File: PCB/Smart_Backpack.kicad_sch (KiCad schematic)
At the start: 5 parts, among them U1 ESP32-PICO-MINI-02-N8R2

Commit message: Add files via upload
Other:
- added sheet Components (untitled.kicad_sch)
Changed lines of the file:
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@@
+		)
+	)
+	(sheet
+		(at 208.28 21.59)
+		(size 13.97 7.62)
+		(exclude_from_sim no)
+		(in_bom yes)
+		(on_board yes)
+		(dnp no)
+		(fields_autoplaced yes)
+		(stroke
+			(width 0.1524)
+			(type solid)
+		)
+		(fill
+			(color 0 0 0 0.0000)
+		)
+		(property "Sheetname" "Components"
+			(at 208.28 20.8784 0)
+			(effects
+				(font
+					(size 1.27 1.27)
+				)
+				(justify left bottom)
+			)
+		)
+		(property "Sheetfile" "untitled.kicad_sch"
+			(at 208.28 29.7946 0)
+			(effects
+				(font
+					(size 1.27 1.27)
+				)
+				(justify left top)
+			)
+		)
+		(instances
+			(project "Smart_Backpack"
+				(path "/38abc652-c887-4ef7-a45f-d93ca7f4b2d6"
+					(page "3")
+				)
+			)
 		)
 	)

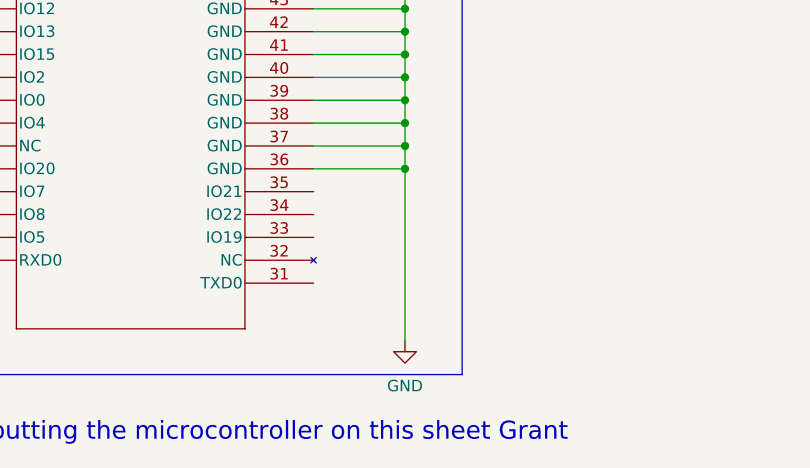
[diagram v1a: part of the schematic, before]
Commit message: Added IMU footprint/symbol
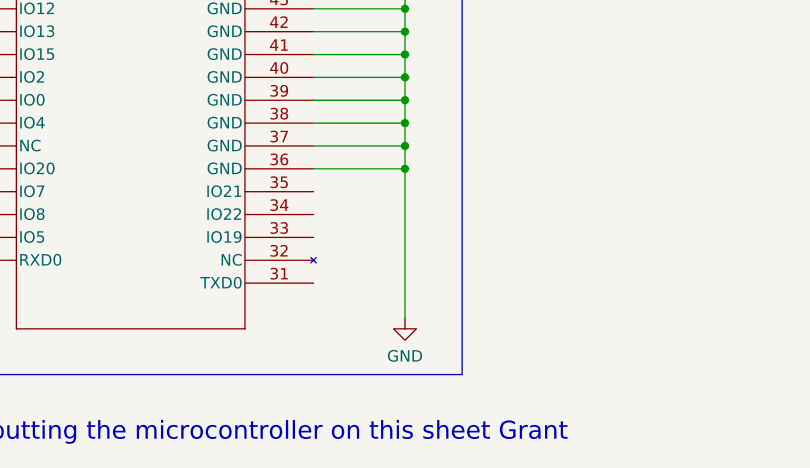
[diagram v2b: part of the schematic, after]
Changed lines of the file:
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@@
 	(wire
 		(pts
-			(xy 78.74 118.11) (xy 78.74 99.06)
+			(xy 78.74 115.57) (xy 78.74 99.06)
 		)
 		(stroke
@@
 	(symbol
 		(lib_id "power:GND")
-		(at 78.74 118.11 0)
+		(at 78.74 115.57 0)
 		(unit 1)
 		(exclude_from_sim no)
@@
 		(on_board yes)
 		(dnp no)
-		(fields_autoplaced yes)
 		(property "Reference" "#PWR02"
-			(at 78.74 124.46 0)
+			(at 78.74 121.92 0)
 			(effects
 				(font
@@
 		)
 		(property "Value" "GND"
-			(at 78.74 123.19 0)
+			(at 78.74 119.888 0)
 			(effects
 				(font
@@
 		)
 		(property "Footprint" ""
-			(at 78.74 118.11 0)
+			(at 78.74 115.57 0)
 			(effects
 				(font
@@
 		)
 		(property "Datasheet" ""
-			(at 78.74 118.11 0)
+			(at 78.74 115.57 0)
 			(effects
 				(font
@@
 		)
 		(property "Description" ""
-			(at 78.74 118.11 0)
-			(effects
-				(font
+			(at 78.74 115.57 0)
+			(effects
+				(font

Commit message: update todo list
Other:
- note added: "Fix Power circuit add reset pin"
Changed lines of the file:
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@@
+		)
+	)
+	(text "Fix Power circuit add reset pin"
+		(exclude_from_sim no)
+		(at 197.866 93.218 0)
+		(effects
+			(font
+				(size 1.27 1.27)
+			)
+			(justify left bottom)
 		)
 	)

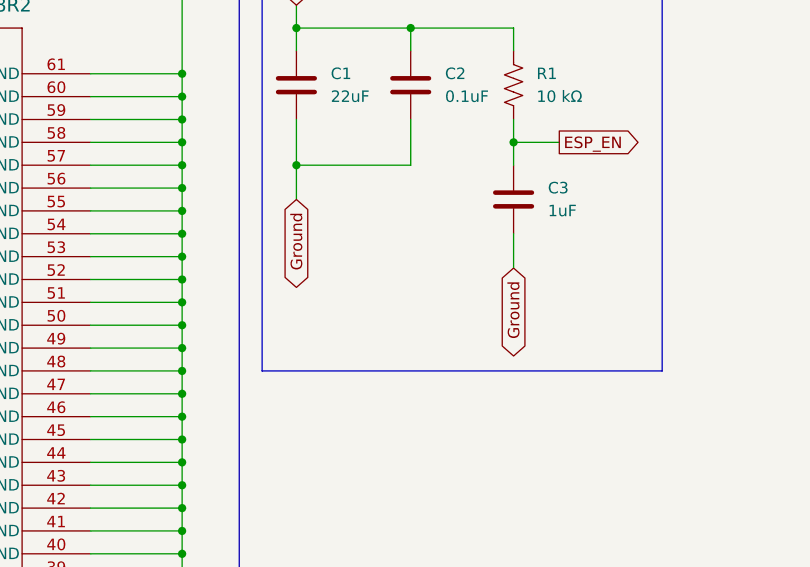
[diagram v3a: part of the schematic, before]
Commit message: Just changed some ground pins to ground
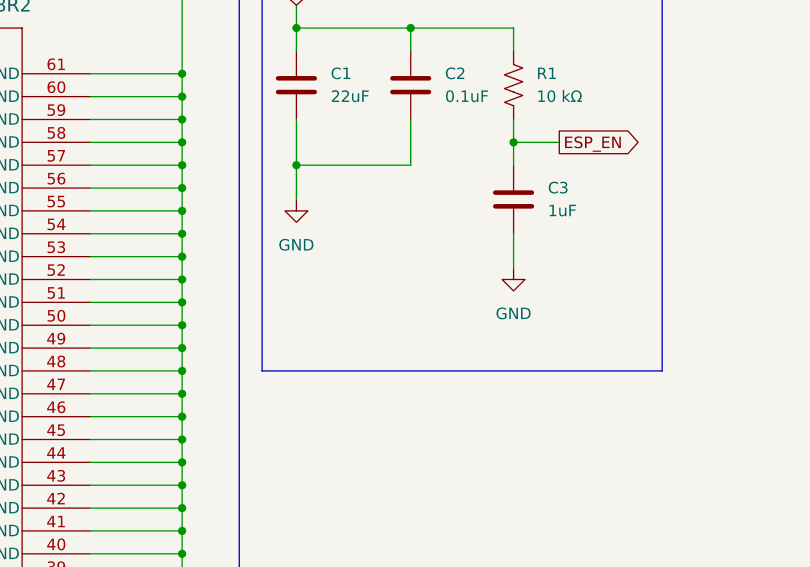
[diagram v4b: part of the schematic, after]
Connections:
- net Ground is gone; now on net GND: C1.2, C2.2, C3.2
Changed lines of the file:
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@@
 		)
 	)
-	(global_label "Ground"
-		(shape bidirectional)
-		(at 115.57 57.15 270)
+	(global_label "Buck_3v3"
+		(shape input)
+		(at 27.94 40.64 180)
 		(fields_autoplaced yes)
 		(effects
@@
 		)
 		(property "Intersheetrefs" "${INTERSHEET_REFS}"
-			(at 115.57 67.8987 90)
+			(at 16.0649 40.64 0)
 			(effects
 				(font
@@
 		)
 	)
-	(global_label "Ground"
-		(shape bidirectional)
-		(at 91.44 49.53 270)
+	(global_label "Buck_3v3"
+		(shape input)
+		(at 91.44 27.94 90)
 		(fields_autoplaced yes)
 		(effects
@@
 				(size 1.27 1.27)
 			)
-			(justify right)
-		)
-		(property "Intersheetrefs" "${INTERSHEET_REFS}"
-			(at 91.44 60.2787 90)
-			(effects
-				(font
-					(size 1.27 1.27)
-				)
-				(justify right)
-				(hide yes)
-			)
-		)
-	)
-	(global_label "Buck_3v3"
-		(shape input)
-		(at 27.94 40.64 180)
-		(fields_autoplaced yes)
-		(effects
-			(font
-				(size 1.27 1.27)
-			)
-			(justify right)
-		)
-		(property "Intersheetrefs" "${INTERSHEET_REFS}"
-			(at 16.0649 40.64 0)
-			(effects
-				(font
-					(size 1.27 1.27)
-				)
-				(justify right)
-				(hide yes)
-			)
-		)
-	)
-	(global_label "Buck_3v3"
-		(shape input)
-		(at 91.44 27.94 90)
-		(fields_autoplaced yes)
-		(effects
-			(font
-				(size 1.27 1.27)
-			)
 			(justify left)
 		)
@@
 				(justify left)
 				(hide yes)
+			)
+		)
+	)
+	(symbol
+		(lib_name "GND_1")
+		(lib_id "power:GND")
+		(at 115.57 57.15 0)
+		(unit 1)
+		(exclude_from_sim no)
+		(in_bom yes)
+		(on_board yes)
+		(dnp no)
+		(fields_autoplaced yes)
+		(property "Reference" "#PWR06"
+			(at 115.57 63.5 0)
+			(effects
+				(font
+					(size 1.27 1.27)
+				)
+				(hide yes)
+			)
+		)
+		(property "Value" "GND"
+			(at 115.57 62.23 0)
+			(effects
+				(font
+					(size 1.27 1.27)
+				)
+			)
+		)
+		(property "Footprint" ""
+			(at 115.57 57.15 0)
+			(effects
+				(font
+					(size 1.27 1.27)
+				)
+				(hide yes)
+			)
+		)
+		(property "Datasheet" ""
+			(at 115.57 57.15 0)
+			(effects
+				(font
+					(size 1.27 1.27)
+				)
+				(hide yes)
+			)
+		)
+		(property "Description" "Power symbol creates a global label with name \"GND\" , ground"
+			(at 115.57 57.15 0)
+			(effects
+				(font
+					(size 1.27 1.27)
+				)
+				(hide yes)
+			)
+		)
+		(pin "1"
+		)
+		(instances
+			(project ""
+				(path "/38abc652-c887-4ef7-a45f-d93ca7f4b2d6"
+					(reference "#PWR06")
+					(unit 1)
+				)
 			)
 		)
@@
 					(unit 1)
 				)
+			)
+		)
+	)
+	(symbol
+		(lib_name "GND_1")
+		(lib_id "power:GND")
+		(at 91.44 49.53 0)
+		(unit 1)
+		(exclude_from_sim no)
+		(in_bom yes)
+		(on_board yes)
+		(dnp no)
+		(fields_autoplaced yes)
+		(property "Reference" "#PWR07"
+			(at 91.44 55.88 0)
+			(effects
+				(font
+					(size 1.27 1.27)
+				)
+				(hide yes)
+			)
+		)
+		(property "Value" "GND"
+			(at 91.44 54.61 0)
+			(effects
+				(font
+					(size 1.27 1.27)
+				)
+			)
+		)
+		(property "Footprint" ""
+			(at 91.44 49.53 0)
+			(effects
+				(font
+					(size 1.27 1.27)
+				)
+				(hide yes)
+			)
+		)
+		(property "Datasheet" ""
+			(at 91.44 49.53 0)
+			(effects
+				(font
+					(size 1.27 1.27)
+				)
+				(hide yes)
+			)
+		)
+		(property "Description" "Power symbol creates a global label with name \"GND\" , ground"
+			(at 91.44 49.53 0)
+			(effects
+				(font
+					(size 1.27 1.27)
+				)
+				(hide yes)
+			)
+		)
+		(pin "1"
+		)
+		(instances
+			(project "Smart_Backpack"
+				(path "/38abc652-c887-4ef7-a45f-d93ca7f4b2d6"
+					(reference "#PWR07")
+					(unit 1)
+				)

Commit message: Added micro footprint
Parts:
- removed U1: ESP32-PICO-MINI-02-N8R2, ESP32:ESP32-PICO-MINI-02_EXP, symbol ESP32:ESP32-PICO-MINI-02-N8R2
- added U3: ESP32-PICO-MINI-02-N8R2, STM32:ESP32-PICO-MINI-02_EXP, symbol ESP32:ESP32-PICO-MINI-02-N8R2
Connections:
- net Buck_3v3: now also U3.3 (3V3)
- net ESP_EN: now also U3.8 (EN)
- net GND: now also U3.1 (GND), U3.11 (GND), U3.14 (GND), U3.2 (GND), U3.36 (GND), U3.37 (GND), U3.38 (GND), U3.39 (GND), U3.40 (GND), U3.41 (GND), U3.42 (GND), U3.43 (GND), U3.44 (GND), U3.45 (GND), U3.46 (GND), U3.47 (GND), U3.48 (GND), U3.49 (GND), U3.50 (GND), U3.51 (GND), U3.52 (GND), U3.53 (GND), U3.54 (GND), U3.55 (GND), U3.56 (GND), U3.57 (GND), U3.58 (GND), U3.59 (GND), U3.60 (GND), U3.61 (GND)
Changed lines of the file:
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@@
+	)
+	(symbol
+		(lib_id "ESP32:ESP32-PICO-MINI-02-N8R2")
+		(at 27.94 35.56 0)
+		(unit 1)
+		(exclude_from_sim no)
+		(in_bom yes)
+		(on_board yes)
+		(dnp no)
+		(fields_autoplaced yes)
+		(property "Reference" "U3"
+			(at 48.26 25.4 0)
+			(effects
+				(font
+					(size 1.524 1.524)
+				)
+			)
+		)
+		(property "Value" "ESP32-PICO-MINI-02-N8R2"
+			(at 48.26 27.94 0)
+			(effects
+				(font
+					(size 1.524 1.524)
+				)
+			)
+		)
+		(property "Footprint" "STM32:ESP32-PICO-MINI-02_EXP"
+			(at 27.94 35.56 0)
+			(effects
+				(font
+					(size 1.27 1.27)
+					(italic yes)
+				)
+				(hide yes)
+			)
+		)
+		(property "Datasheet" "ESP32-PICO-MINI-02-N8R2"
+			(at 27.94 35.56 0)
+			(effects
+				(font
+					(size 1.27 1.27)
+					(italic yes)
+				)
+				(hide yes)
+			)
+		)
+		(property "Description" ""
+			(at 27.94 35.56 0)
+			(effects
+				(font
+					(size 1.27 1.27)
+				)
+				(hide yes)
+			)
+		)
+		(pin "1"
+		)
+		(pin "9"
+		)
+		(pin "14"
+		)
+		(pin "13"
+		)
+		(pin "2"
+		)
+		(pin "5"
+		)
+		(pin "23"
+		)
+		(pin "24"
+		)
+		(pin "6"
+		)
+		(pin "17"
+		)
+		(pin "4"
+		)
+		(pin "8"
+		)
+		(pin "11"
+		)
+		(pin "15"
+		)
+		(pin "3"
+		)
+		(pin "7"
+		)
+		(pin "10"
+		)
+		(pin "12"
+		)
+		(pin "16"
+		)
+		(pin "19"
+		)
+		(pin "18"
+		)
+		(pin "20"
+		)
+		(pin "21"
+		)
+		(pin "22"
+		)
+		(pin "27"
+		)
+		(pin "61"
+		)
+		(pin "57"
+		)
+		(pin "56"
+		)
+		(pin "29"
+		)
+		(pin "59"
+		)
+		(pin "25"
+		)
+		(pin "26"
+		)
+		(pin "28"
+		)
+		(pin "30"
+		)
+		(pin "60"
+		)
+		(pin "58"
+		)
+		(pin "52"
+		)
+		(pin "39"
+		)
+		(pin "54"
+		)
+		(pin "47"
+		)
+		(pin "33"
+		)
+		(pin "32"
+		)
+		(pin "49"
+		)
+		(pin "55"
+		)
+		(pin "51"
+		)
+		(pin "50"
+		)
+		(pin "48"
+		)
+		(pin "53"
+		)
+		(pin "44"
+		)
+		(pin "43"
+		)
+		(pin "45"
+		)
+		(pin "46"
+		)
+		(pin "42"
+		)
+		(pin "41"
+		)
+		(pin "38"
+		)
+		(pin "40"
+		)
+		(pin "37"
+		)
+		(pin "36"
+		)
+		(pin "35"
+		)
+		(pin "34"
+		)
+		(pin "31"
+		)
+		(instances
+			(project ""
+				(path "/38abc652-c887-4ef7-a45f-d93ca7f4b2d6"
+					(reference "U3")
+					(unit 1)
+				)
+			)
+		)
 	)
 	(symbol
@@
 					(unit 1)
 				)
-			)
-		)
-	)
-	(symbol
-		(lib_id "ESP32:ESP32-PICO-MINI-02-N8R2")
-		(at 27.94 35.56 0)
-		(unit 1)
-		(exclude_from_sim no)
-		(in_bom yes)
-		(on_board yes)
-		(dnp no)
-		(fields_autoplaced yes)
-		(property "Reference" "U1"
-			(at 48.26 25.4 0)
-			(effects
-				(font
-					(size 1.524 1.524)
-				)
-			)
-		)
-		(property "Value" "ESP32-PICO-MINI-02-N8R2"
-			(at 48.26 27.94 0)
-			(effects
-				(font
-					(size 1.524 1.524)
-				)
-			)
-		)
-		(property "Footprint" "ESP32:ESP32-PICO-MINI-02_EXP"
-			(at 27.94 35.56 0)
-			(effects
-				(font
-					(size 1.27 1.27)
-					(italic yes)
-				)
-				(hide yes)
-			)
-		)
-		(property "Datasheet" "ESP32-PICO-MINI-02-N8R2"
-			(at 27.94 35.56 0)
-			(effects
-				(font
-					(size 1.27 1.27)
-					(italic yes)
-				)
-				(hide yes)
-			)
-		)
-		(property "Description" ""
-			(at 27.94 35.56 0)
-			(effects
-				(font
-					(size 1.27 1.27)
-				)
-			)
-		)
-		(pin "24"
-		)
-		(pin "6"
-		)
-		(pin "34"
-		)
-		(pin "36"
-		)
-		(pin "39"
-		)
-		(pin "48"
-		)
-		(pin "18"
-		)
-		(pin "10"
-		)
-		(pin "57"
-		)
-		(pin "47"
-		)
-		(pin "28"
-		)
-		(pin "33"
-		)
-		(pin "53"
-		)
-		(pin "7"
-		)
-		(pin "25"
-		)
-		(pin "59"
-		)
-		(pin "44"
-		)
-		(pin "31"
-		)
-		(pin "35"
-		)
-		(pin "14"
-		)
-		(pin "17"
-		)
-		(pin "27"
-		)
-		(pin "55"
-		)
-		(pin "30"
-		)
-		(pin "56"
-		)
-		(pin "15"
-		)
-		(pin "22"
-		)
-		(pin "38"
-		)
-		(pin "52"
-		)
-		(pin "58"
-		)
-		(pin "60"
-		)
-		(pin "13"
-		)
-		(pin "21"
-		)
-		(pin "37"
-		)
-		(pin "45"
-		)
-		(pin "19"
-		)
-		(pin "29"
-		)
-		(pin "40"
-		)
-		(pin "50"
-		)
-		(pin "5"
-		)
-		(pin "42"
-		)
-		(pin "26"
-		)
-		(pin "9"
-		)
-		(pin "2"
-		)
-		(pin "20"
-		)
-		(pin "43"
-		)
-		(pin "3"
-		)
-		(pin "23"
-		)
-		(pin "1"
-		)
-		(pin "16"
-		)
-		(pin "32"
-		)
-		(pin "12"
-		)
-		(pin "46"
-		)
-		(pin "49"
-		)
-		(pin "11"
-		)
-		(pin "41"
-		)
-		(pin "4"
-		)
-		(pin "51"
-		)
-		(pin "54"
-		)
-		(pin "61"
-		)
-		(pin "8"
-		)
-		(instances
-			(project "Smart_Backpack"
-				(path "/38abc652-c887-4ef7-a45f-d93ca7f4b2d6"
-					(reference "U1")
-					(unit 1)
-				)

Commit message: work on IMU
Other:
- sheet Components renamed IMU
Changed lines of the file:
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@@
 			(color 0 0 0 0.0000)
 		)
-		(property "Sheetname" "Components"
+		(property "Sheetname" "IMU"
 			(at 208.28 20.8784 0)
 			(effects

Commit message: IMU done yay
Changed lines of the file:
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@@
 		(fields_autoplaced yes)
 		(property "Reference" "R1"
-			(at 118.11 35.56 0)
+			(at 118.11 35.5599 0)
 			(effects
 				(font
@@
 		)
 		(property "Value" "10 kΩ"
-			(at 118.11 38.1 0)
+			(at 118.11 38.0999 0)
 			(effects
 				(font

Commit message: add pressure button and R, C, and L footprints
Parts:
- added H3, H4, H5, H6: MountingHole, MountingHole:MountingHole_3mm, symbol Mechanical:MountingHole
- C1, C2, C3: footprint (none) -> Capacitor_SMD:C_1206_3216Metric_Pad1.33x1.80mm_HandSolder
- R1: footprint (none) -> Resistor_SMD:R_1206_3216Metric_Pad1.30x1.75mm_HandSolder
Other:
- sheet IMU renamed Peripherals
- sheet Peripherals: file untitled.kicad_sch -> peripherals.kicad_sch
- note added: "Mounting Holes"
- note removed: "Connections for off board components"
- note removed: "GPS maybe? If we can get an external antenna, GPS on PCB"
- note removed: "I'm just putting the microcontroller on this sheet Grant"
